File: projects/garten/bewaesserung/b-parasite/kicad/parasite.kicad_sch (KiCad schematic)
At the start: 29 parts, among them Q1 MMBT3906, Q4 Q_Photo_NPN, SW1 B3U-1000P, U1 E73-2G4M08S1C, U2 SHTC3, Y1 32.768kHz

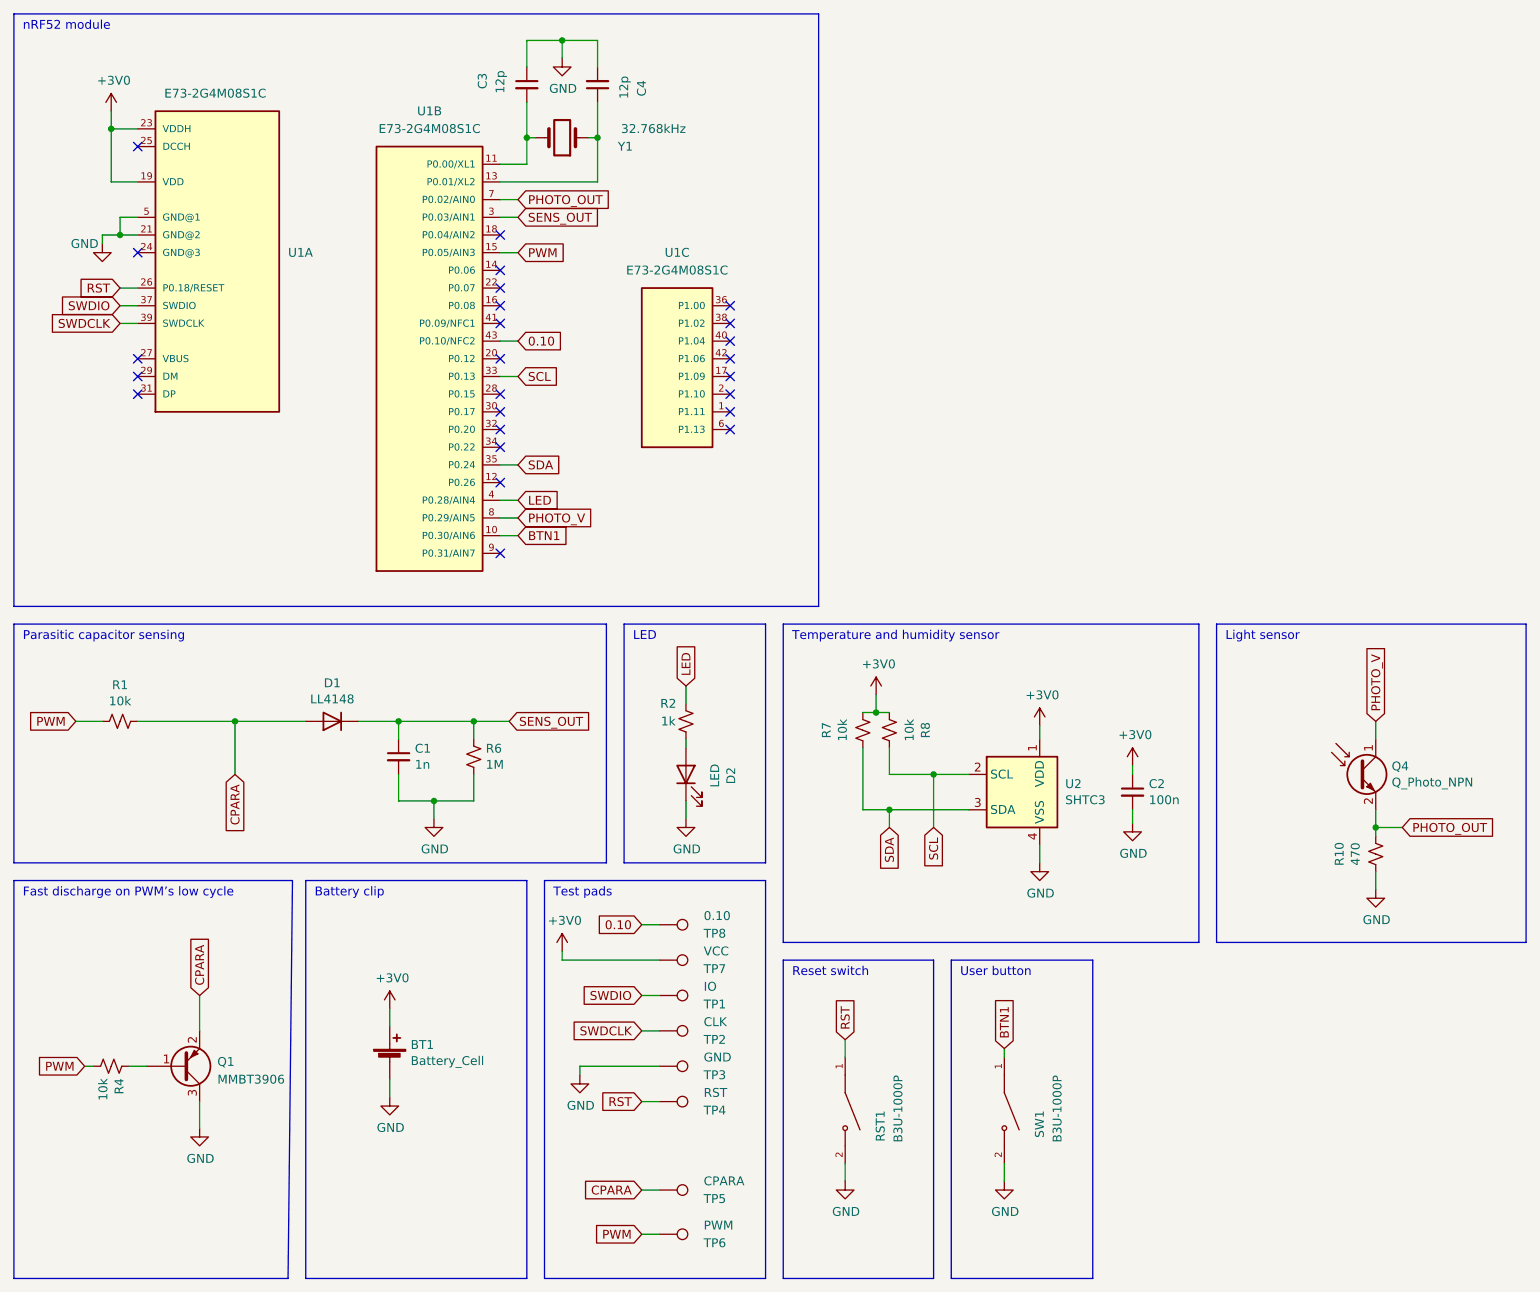
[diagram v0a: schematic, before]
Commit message: [garten/bewaesserung/b-parasite(pcb)] fix all ERC violations
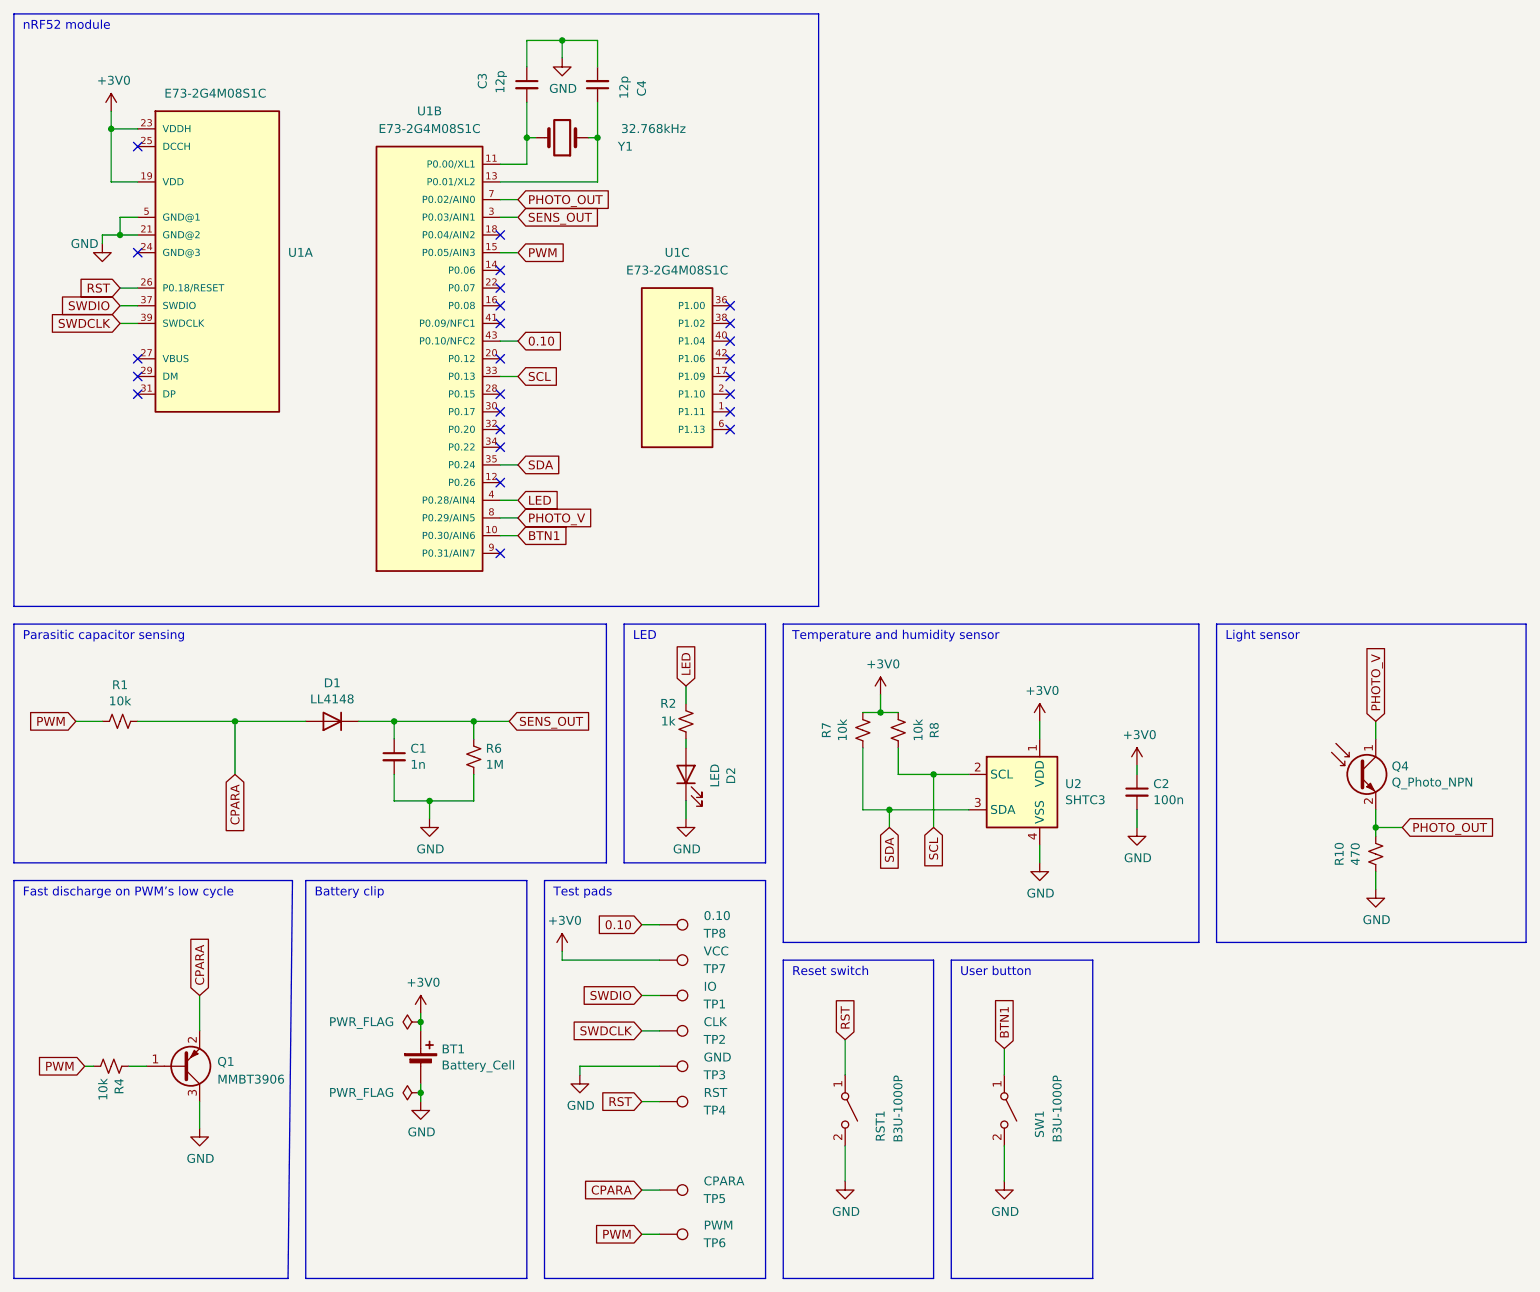
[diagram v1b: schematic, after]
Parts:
- BT1: footprint kicad:BatteryHolder_Keystone_3002_1x2032 -> tme:BatteryHolder_Keystone_3002_1x2032
- RST1, SW1: footprint SW_B3U-1000P -> Button_Switch_SMD:SW_SPST_B3U-1000P; symbol B3U-1000P:B3U-1000P -> Switch:SW_SPST
- U1: symbol E73:E73-2G4M08S1C -> E73-2G4M08S1C:E73-2G4M08S1C
- U1: symbol E73:E73-2G4M08S1C -> E73-2G4M08S1C:E73-2G4M08S1C; LCSC C356849 -> (none)
- U2: footprint kicad:Sensirion_DFN-4-1EP_2x2mm_P1mm_EP0.7x1.6mm -> Sensor_Humidity:Sensirion_DFN-4-1EP_2x2mm_P1mm_EP0.7x1.6mm
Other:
- moved on the sheet: BT1, C1, C2, R8

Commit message: [garten/bewaesserung/b-parasite(pcb)] add mpn to easier order pcb
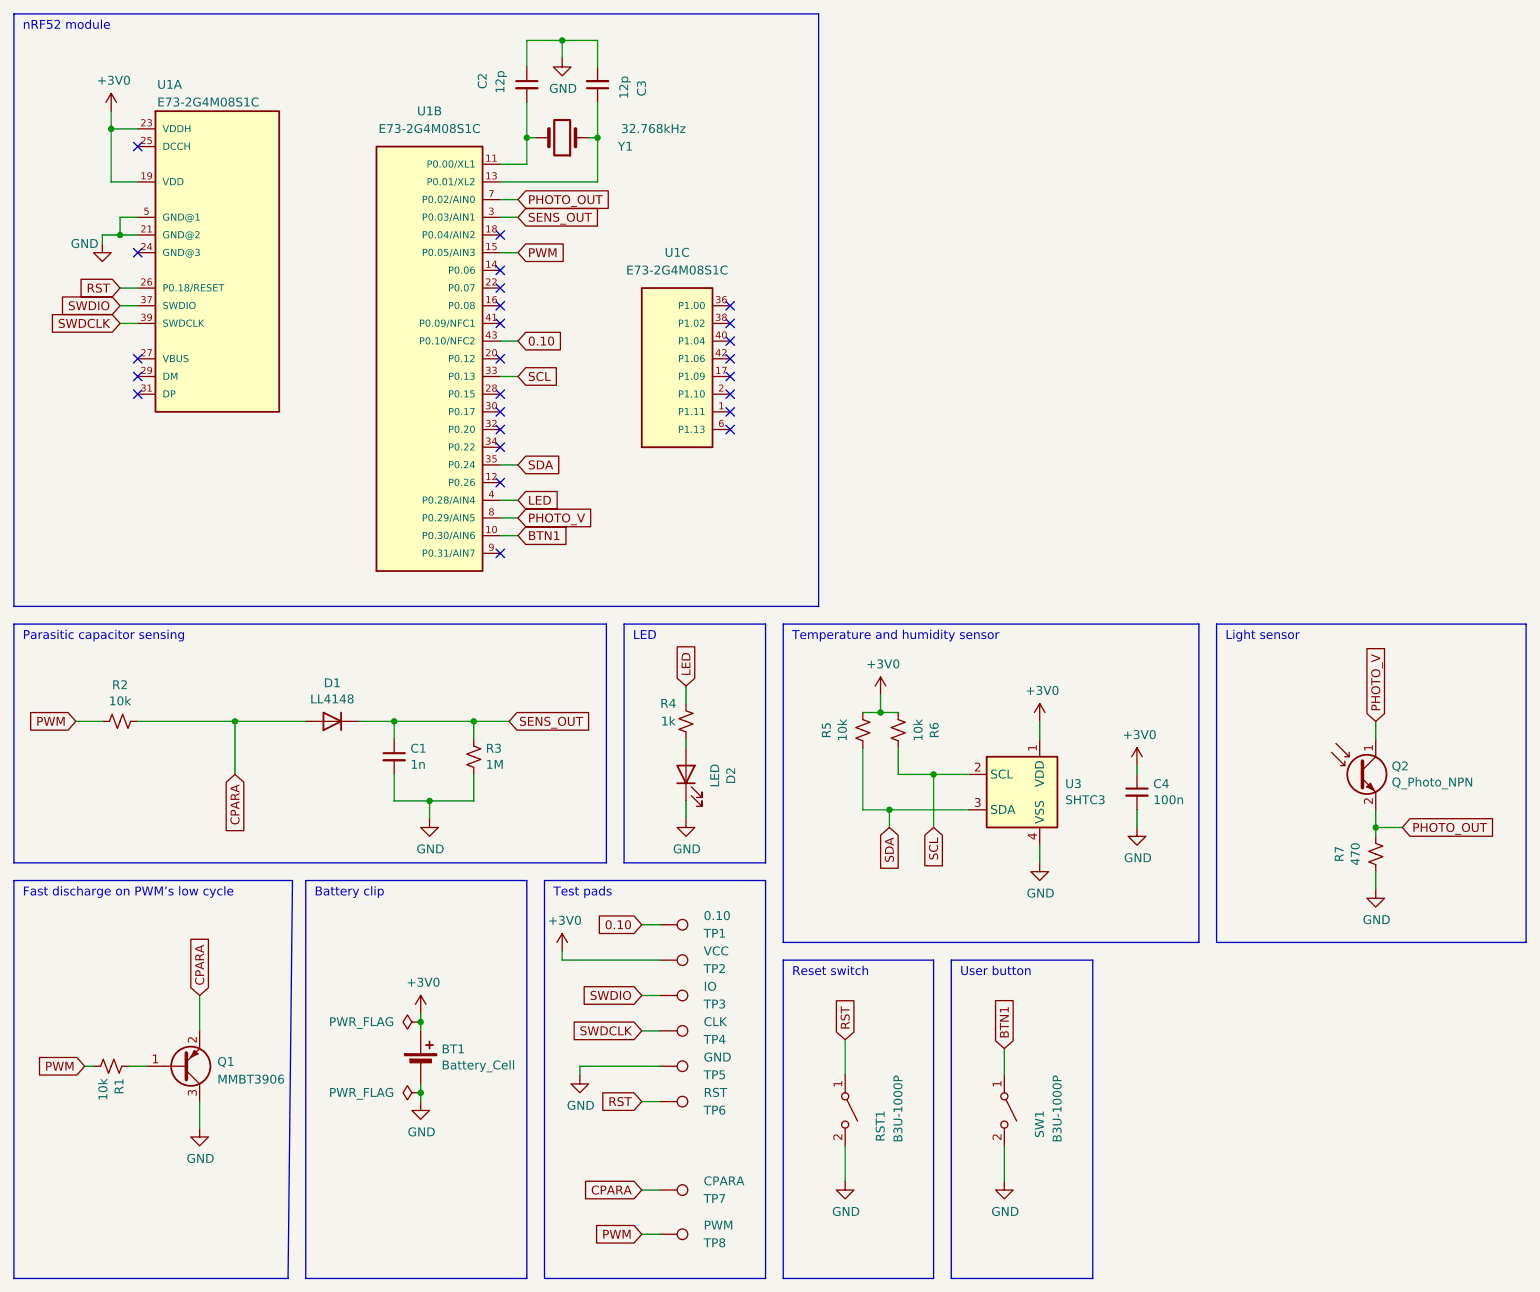
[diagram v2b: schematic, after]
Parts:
- BT1: MPN (none) -> 3002TR
- C2: renamed from C3; MPN (none) -> GRM1555C1H120GA01D
- C3: renamed from C4; MPN (none) -> GRM1555C1H120GA01D
- C4: renamed from C2; MPN (none) -> GRM155R71A104KA01D
- D1: MPN (none) -> LL4148-GS18
- Q1: MPN (none) -> PZT3906
- Q2: renamed from Q4; MPN (none) -> ALS-PT19-315C/L177/TR8
- R1: renamed from R4; MPN (none) -> CRGCQ0402F10K
- R2: renamed from R1; MPN (none) -> CRGCQ0402F10K
- R3: renamed from R6; MPN (none) -> CRGCQ0402F1M0
- R4: renamed from R2; MPN (none) -> CRGCQ0402F1K0
- R5: renamed from R7; MPN (none) -> CRGCQ0402F10K
- R6: renamed from R8; MPN (none) -> CRGCQ0402F10K
- R7: renamed from R10; MPN (none) -> RLP73N1ER47FTDF
- RST1, SW1: MPN (none) -> B3U-1000P
- U1: MPN (none) -> E73-2G4M08S1C
- Y1: MPN (none) -> FC-135 32.7680KA-AC0
- renumbered TP8 to TP1, TP7 to TP2, TP1 to TP3, TP2 to TP4, TP3 to TP5, TP4 to TP6, TP5 to TP7, TP6 to TP8, U2 to U3
